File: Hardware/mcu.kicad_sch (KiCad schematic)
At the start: 7 parts, among them Q1 BSS138DW-7-F, U6 AS7341-DLGT

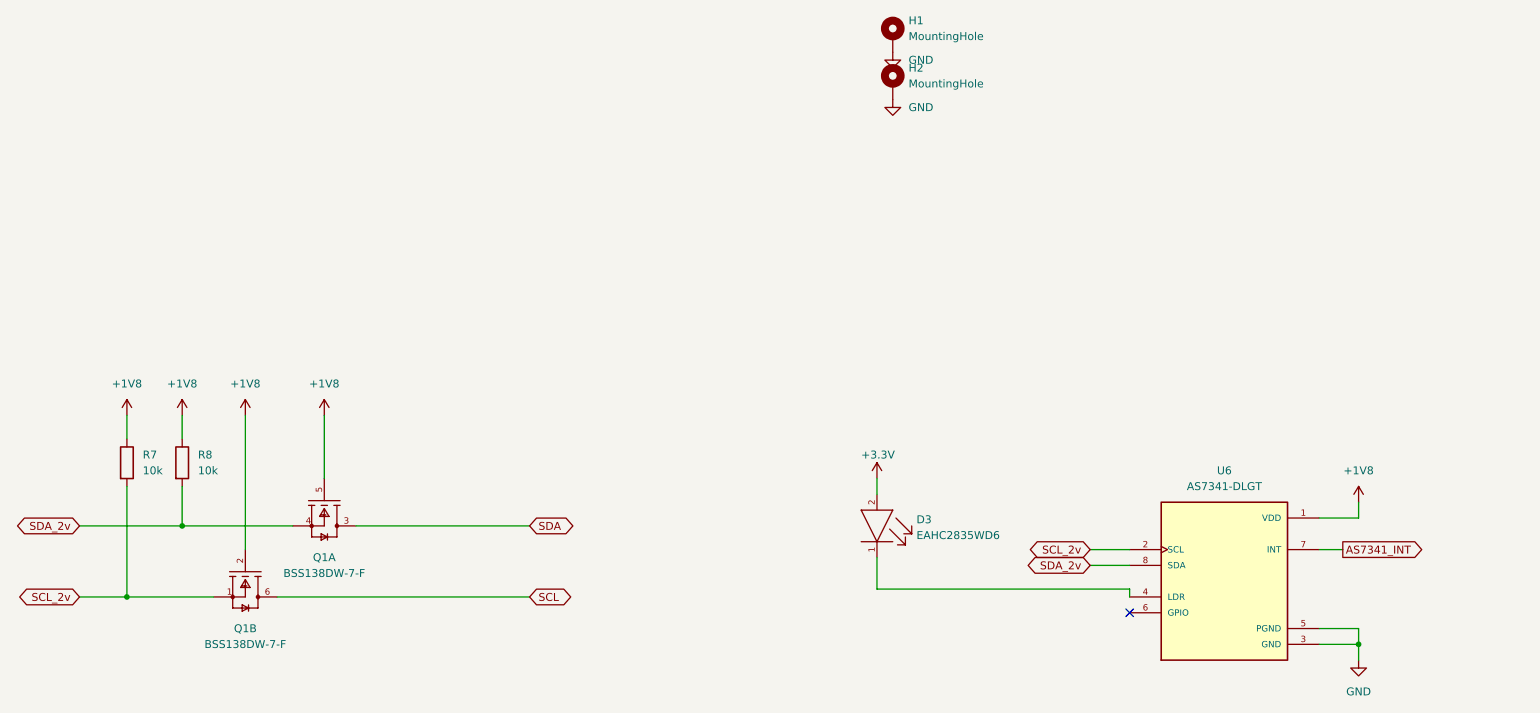
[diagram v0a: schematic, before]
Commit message: Added pullup resistor to AS7341_INT line
Signed-off-by: lokimetasmith <lokimail@gmail.com>
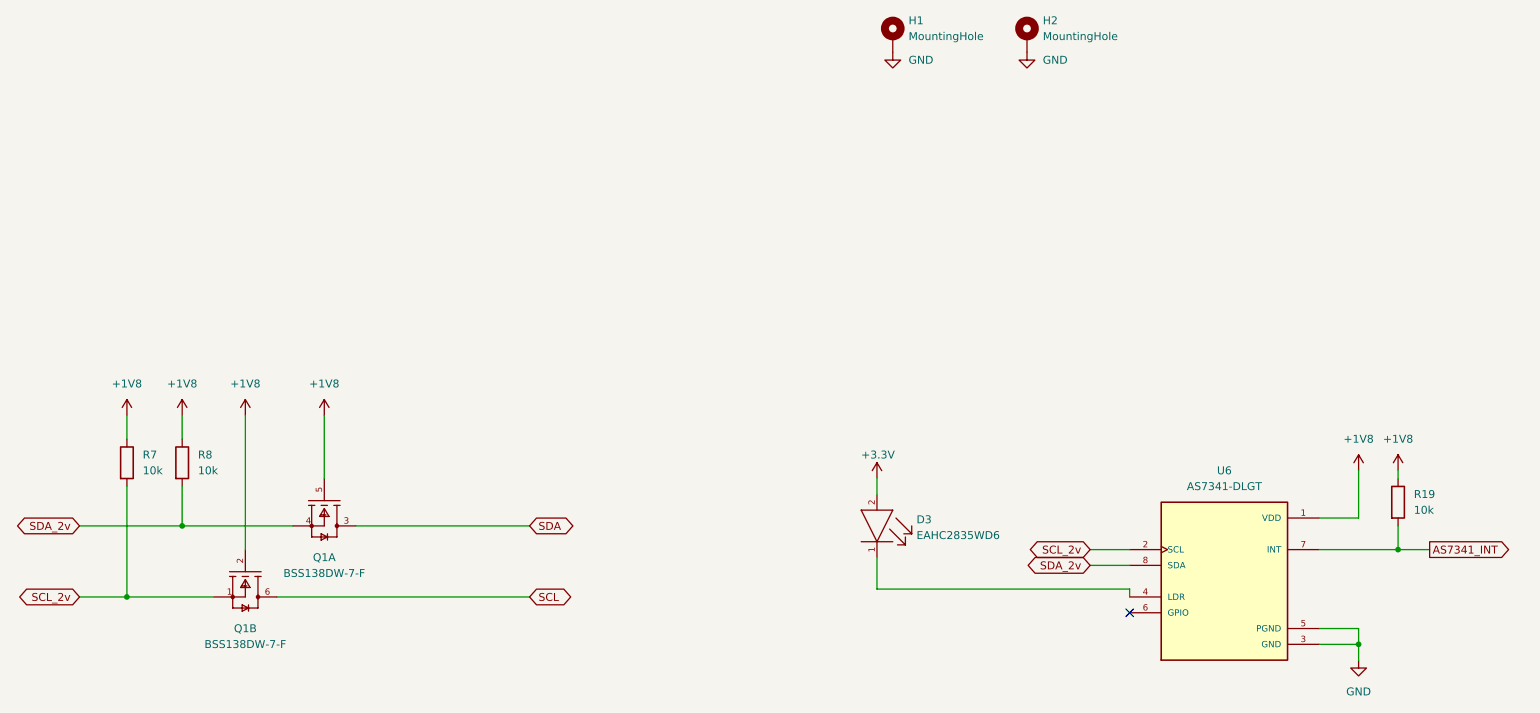
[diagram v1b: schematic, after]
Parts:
- added R19: 10k, Resistor_SMD:R_0603_1608Metric_Pad0.98x0.95mm_HandSolder, symbol Device:R
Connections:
- net +1V8: now also R19.1
- net AS7341_INT: now also R19.2
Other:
- moved on the sheet: H2
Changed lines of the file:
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@@
   (junction (at 59.69 121.92) (diameter 0) (color 0 0 0 0)
+  )
+  (junction (at 264.16 114.3) (diameter 0) (color 0 0 0 0)
   )
   (junction (at 68.58 110.49) (diameter 0) (color 0 0 0 0)
@@
     (stroke (width 0) (type default) (color 0 0 0 0))
   )
-  (wire (pts (xy 257.81 106.68) (xy 257.81 109.22))
+  (wire (pts (xy 257.81 101.6) (xy 257.81 109.22))
     (stroke (width 0) (type default) (color 0 0 0 0))
   )
@@
     (stroke (width 0) (type default) (color 0 0 0 0))
   )
+  (wire (pts (xy 264.16 110.49) (xy 264.16 114.3))
+    (stroke (width 0) (type default) (color 0 0 0 0))
+  )
   (wire (pts (xy 96.52 110.49) (xy 124.46 110.49))
     (stroke (width 0) (type default) (color 0 0 0 0))
@@
     (stroke (width 0) (type default) (color 0 0 0 0))
   )
+  (wire (pts (xy 264.16 114.3) (xy 269.24 114.3))
+    (stroke (width 0) (type default) (color 0 0 0 0))
+  )
+  (wire (pts (xy 264.16 101.6) (xy 264.16 102.87))
+    (stroke (width 0) (type default) (color 0 0 0 0))
+  )
   (wire (pts (xy 214.63 116.84) (xy 220.98 116.84))
     (stroke (width 0) (type default) (color 0 0 0 0))
@@
     (stroke (width 0) (type default) (color 0 0 0 0))
   )
-  (wire (pts (xy 251.46 114.3) (xy 255.27 114.3))
+  (wire (pts (xy 251.46 114.3) (xy 264.16 114.3))
     (stroke (width 0) (type default) (color 0 0 0 0))
   )
@@
     )
   )
-  (global_label "AS7341_INT" (shape output) (at 255.27 114.3 0) (fields_autoplaced)
+  (global_label "AS7341_INT" (shape output) (at 269.24 114.3 0) (fields_autoplaced)
     (effects (font (size 1.27 1.27)) (justify left))
-    (property "Intersheet References" "${INTERSHEET_REFS}" (id 0) (at 268.6898 114.2206 0)
+    (property "Intersheet References" "${INTERSHEET_REFS}" (id 0) (at 282.6598 114.2206 0)
       (effects (font (size 1.27 1.27)) (justify left) hide)
     )
@@
     (pin "1")
   )
-  (symbol (lib_id "Mechanical:MountingHole_Pad") (at 182.88 39.37 0) (unit 1)
-    (in_bom yes) (on_board yes) (fields_autoplaced)
-    (property "Reference" "H2" (id 0) (at 185.42 36.8299 0)
-      (effects (font (size 1.27 1.27)) (justify left))
-    )
-    (property "Value" "MountingHole" (id 1) (at 185.42 39.3699 0)
-      (effects (font (size 1.27 1.27)) (justify left))
-    )
-    (property "Footprint" "MountingHole:MountingHole_2.2mm_M2_ISO7380_Pad" (id 2) (at 182.88 39.37 0)
-      (effects (font (size 1.27 1.27)) hide)
-    )
-    (property "Datasheet" "~" (id 3) (at 182.88 39.37 0)
+  (symbol (lib_id "Mechanical:MountingHole_Pad") (at 204.47 31.75 0) (unit 1)
+    (in_bom yes) (on_board yes) (fields_autoplaced)
+    (property "Reference" "H2" (id 0) (at 207.01 29.2099 0)
+      (effects (font (size 1.27 1.27)) (justify left))
+    )
+    (property "Value" "MountingHole" (id 1) (at 207.01 31.7499 0)
+      (effects (font (size 1.27 1.27)) (justify left))
+    )
+    (property "Footprint" "MountingHole:MountingHole_2.2mm_M2_ISO7380_Pad" (id 2) (at 204.47 31.75 0)
+      (effects (font (size 1.27 1.27)) hide)
+    )
+    (property "Datasheet" "~" (id 3) (at 204.47 31.75 0)
       (effects (font (size 1.27 1.27)) hide)
     )
@@
     )
     (pin "1")
+  )
+  (symbol (lib_id "Device:R") (at 264.16 106.68 0) (unit 1)
+    (in_bom yes) (on_board yes) (fields_autoplaced)
+    (property "Reference" "R19" (id 0) (at 266.7 105.4099 0)
+      (effects (font (size 1.27 1.27)) (justify left))
+    )
+    (property "Value" "10k" (id 1) (at 266.7 107.9499 0)
+      (effects (font (size 1.27 1.27)) (justify left))
+    )
+    (property "Footprint" "Resistor_SMD:R_0603_1608Metric_Pad0.98x0.95mm_HandSolder" (id 2) (at 262.382 106.68 90)
+      (effects (font (size 1.27 1.27)) hide)
+    )
+    (property "Datasheet" "~" (id 3) (at 264.16 106.68 0)
+      (effects (font (size 1.27 1.27)) hide)
+    )
+    (pin "1")
+    (pin "2")
   )
   (symbol (lib_id "power:+1V8") (at 91.44 92.71 0) (unit 1)
@@
     (pin "1")
   )
-  (symbol (lib_id "power:+1V8") (at 257.81 106.68 0) (unit 1)
-    (in_bom yes) (on_board yes) (fields_autoplaced)
-    (property "Reference" "#PWR0114" (id 0) (at 257.81 110.49 0)
-      (effects (font (size 1.27 1.27)) hide)
-    )
-    (property "Value" "+1V8" (id 1) (at 257.81 101.6 0))
-    (property "Footprint" "" (id 2) (at 257.81 106.68 0)
-      (effects (font (size 1.27 1.27)) hide)
-    )
-    (property "Datasheet" "" (id 3) (at 257.81 106.68 0)
+  (symbol (lib_id "power:+1V8") (at 264.16 101.6 0) (unit 1)
+    (in_bom yes) (on_board yes) (fields_autoplaced)
+    (property "Reference" "#PWR0116" (id 0) (at 264.16 105.41 0)
+      (effects (font (size 1.27 1.27)) hide)
+    )
+    (property "Value" "+1V8" (id 1) (at 264.16 96.52 0))
+    (property "Footprint" "" (id 2) (at 264.16 101.6 0)
+      (effects (font (size 1.27 1.27)) hide)
+    )
+    (property "Datasheet" "" (id 3) (at 264.16 101.6 0)
+      (effects (font (size 1.27 1.27)) hide)
+    )
+    (pin "1")
+  )
+  (symbol (lib_id "power:+1V8") (at 257.81 101.6 0) (unit 1)
+    (in_bom yes) (on_board yes)
+    (property "Reference" "#PWR0114" (id 0) (at 257.81 105.41 0)
+      (effects (font (size 1.27 1.27)) hide)
+    )
+    (property "Value" "+1V8" (id 1) (at 257.81 96.52 0))
+    (property "Footprint" "" (id 2) (at 257.81 101.6 0)
+      (effects (font (size 1.27 1.27)) hide)
+    )
+    (property "Datasheet" "" (id 3) (at 257.81 101.6 0)
       (effects (font (size 1.27 1.27)) hide)
     )
@@
     (pin "1")
   )
-  (symbol (lib_id "power:GND") (at 182.88 41.91 0) (unit 1)
-    (in_bom yes) (on_board yes) (fields_autoplaced)
-    (property "Reference" "#PWR0108" (id 0) (at 182.88 48.26 0)
-      (effects (font (size 1.27 1.27)) hide)
-    )
-    (property "Value" "GND" (id 1) (at 185.42 43.1799 0)
-      (effects (font (size 1.27 1.27)) (justify left))
-    )
-    (property "Footprint" "" (id 2) (at 182.88 41.91 0)
-      (effects (font (size 1.27 1.27)) hide)
-    )
-    (property "Datasheet" "" (id 3) (at 182.88 41.91 0)
-      (effects (font (size 1.27 1.27)) hide)
-    )
+  (symbol (lib_id "power:GND") (at 204.47 34.29 0) (unit 1)
+    (in_bom yes) (on_board yes) (fields_autoplaced)
+    (property "Reference" "#PWR0108" (id 0) (at 204.47 40.64 0)
+      (effects (font (size 1.27 1.27)) hide)
+    )
+    (property "Value" "GND" (id 1) (at 207.01 35.5599 0)
+      (effects (font (size 1.27 1.27)) (justify left))
+    )
+    (property "Footprint" "" (id 2) (at 204.47 34.29 0)
+      (effects (font (size 1.27 1.27)) hide)
+    )
+    (property "Datasheet" "" (id 3) (at 204.47 34.29 0)
+      (effects (font (size 1.27 1.27)) hide)
+    )
